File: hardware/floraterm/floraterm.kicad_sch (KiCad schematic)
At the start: 3 parts, among them U1 TMUX1104DGSR, U2 TMUX1104DGSR

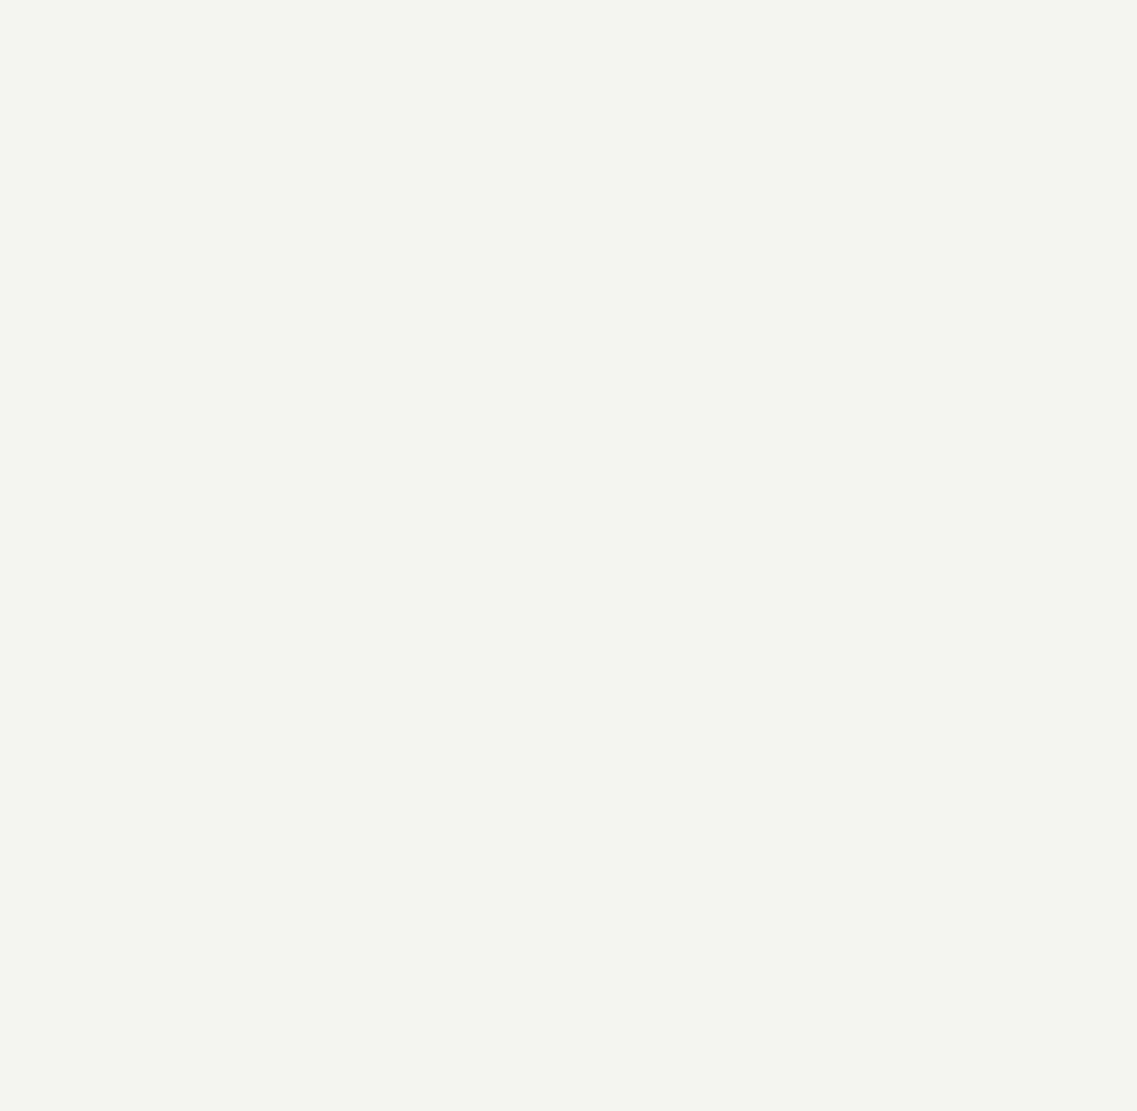
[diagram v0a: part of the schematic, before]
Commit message: add dcdc and bat chrg
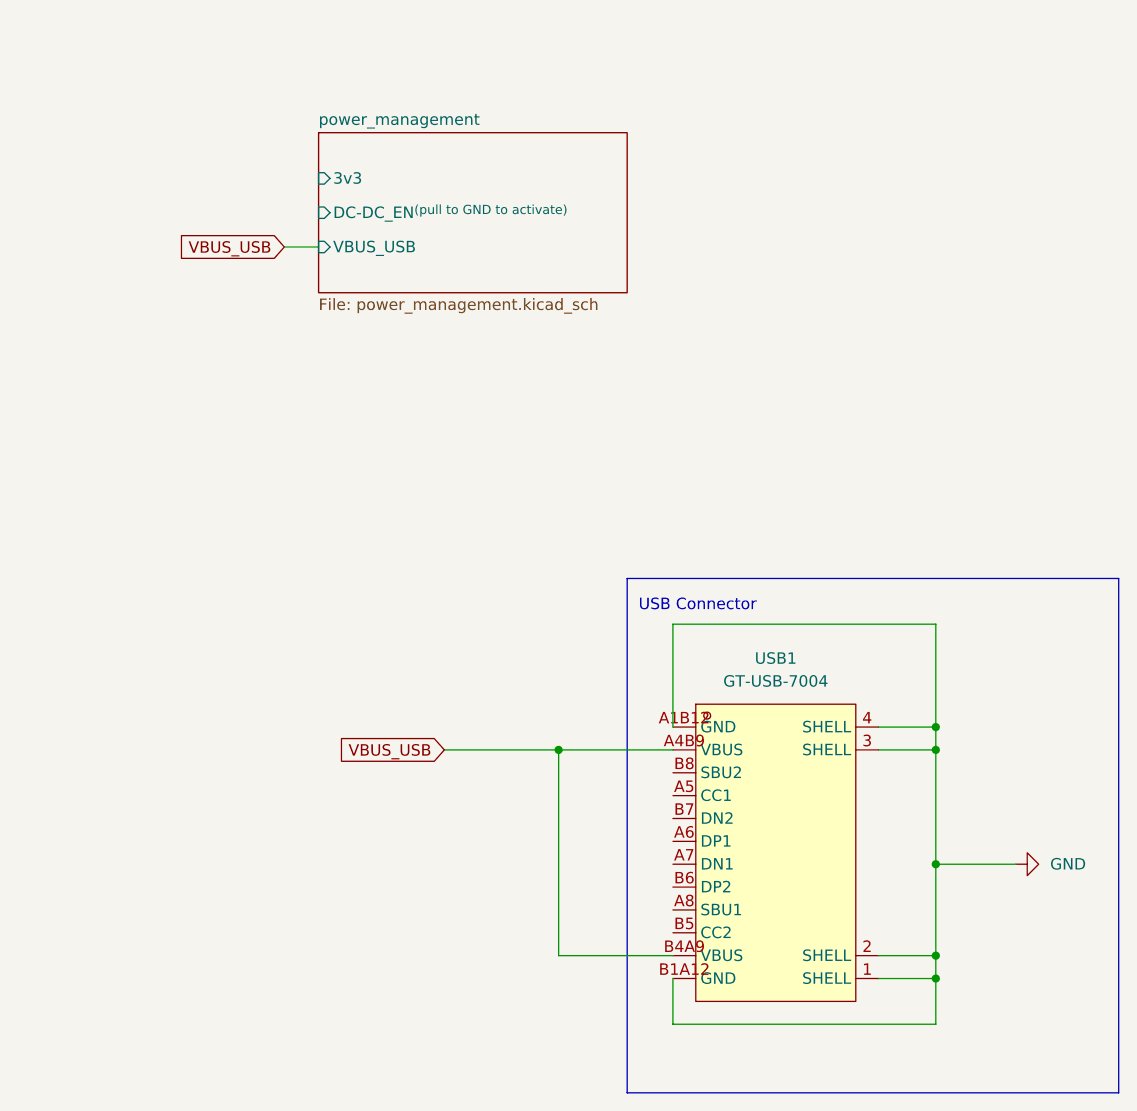
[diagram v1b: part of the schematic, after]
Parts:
- added USB1: GT-USB-7004, lcsc:USB-C-SMD_GT-USB-7004, symbol lcsc:GT-USB-7004
- 1: footprint (none) -> M1s:M1s
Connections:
- new net GND: USB1.1 (SHELL), USB1.2 (SHELL), USB1.3 (SHELL), USB1.4 (SHELL), USB1.A1B12 (GND), USB1.B1A12 (GND)
- new net VBUS_USB: USB1.A4B9 (VBUS), USB1.B4A9 (VBUS)
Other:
- added sheet power_management (power_management.kicad_sch)
- note added: "USB Connector"
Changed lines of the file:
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@@
     (rev "1.0.0")
   )
+  (junction (at 374.65 157.48) (diameter 0) (color 0 0 0 0)
+  )
+  (junction (at 374.65 154.94) (diameter 0) (color 0 0 0 0)
+  )
+  (junction (at 374.65 180.34) (diameter 0) (color 0 0 0 0)
+  )
+  (junction (at 332.74 157.48) (diameter 0) (color 0 0 0 0)
+  )
+  (junction (at 374.65 182.88) (diameter 0) (color 0 0 0 0)
+  )
+  (junction (at 374.65 170.18) (diameter 0) (color 0 0 0 0)
+  )
+  (wire (pts (xy 374.65 157.48) (xy 374.65 170.18))
+    (stroke (width 0) (type default))
+  )
+  (wire (pts (xy 374.65 170.18) (xy 374.65 180.34))
+    (stroke (width 0) (type default))
+  )
+  (wire (pts (xy 345.44 143.51) (xy 374.65 143.51))
+    (stroke (width 0) (type default))
+  )
+  (wire (pts (xy 368.3 180.34) (xy 374.65 180.34))
+    (stroke (width 0) (type default))
+  )
+  (wire (pts (xy 368.3 157.48) (xy 374.65 157.48))
+    (stroke (width 0) (type default))
+  )
+  (wire (pts (xy 345.44 180.34) (xy 332.74 180.34))
+    (stroke (width 0) (type default))
+  )
+  (wire (pts (xy 368.3 154.94) (xy 374.65 154.94))
+    (stroke (width 0) (type default))
+  )
+  (wire (pts (xy 345.44 154.94) (xy 345.44 143.51))
+    (stroke (width 0) (type default))
+  )
+  (wire (pts (xy 368.3 182.88) (xy 374.65 182.88))
+    (stroke (width 0) (type default))
+  )
+  (wire (pts (xy 374.65 154.94) (xy 374.65 157.48))
+    (stroke (width 0) (type default))
+  )
+  (wire (pts (xy 332.74 180.34) (xy 332.74 157.48))
+    (stroke (width 0) (type default))
+  )
+  (wire (pts (xy 374.65 170.18) (xy 383.54 170.18))
+    (stroke (width 0) (type default))
+  )
+  (wire (pts (xy 345.44 187.96) (xy 374.65 187.96))
+    (stroke (width 0) (type default))
+  )
+  (wire (pts (xy 374.65 180.34) (xy 374.65 182.88))
+    (stroke (width 0) (type default))
+  )
+  (wire (pts (xy 374.65 143.51) (xy 374.65 154.94))
+    (stroke (width 0) (type default))
+  )
+  (wire (pts (xy 345.44 182.88) (xy 345.44 187.96))
+    (stroke (width 0) (type default))
+  )
+  (wire (pts (xy 320.04 157.48) (xy 332.74 157.48))
+    (stroke (width 0) (type default))
+  )
+  (wire (pts (xy 302.26 101.6) (xy 306.07 101.6))
+    (stroke (width 0) (type default))
+  )
+  (wire (pts (xy 374.65 182.88) (xy 374.65 187.96))
+    (stroke (width 0) (type default))
+  )
+  (wire (pts (xy 332.74 157.48) (xy 345.44 157.48))
+    (stroke (width 0) (type default))
+  )
+  (rectangle (start 340.36 138.43) (end 394.97 195.58)
+    (stroke (width 0) (type default))
+    (fill (type none))
+  )
   (rectangle (start 39.37 85.09) (end 99.06 161.29)
     (stroke (width 0) (type default))
     (fill (type none))
+  )
+  (text "USB Connector" (at 341.63 142.24 0)
+    (effects (font (size 1.27 1.27)) (justify left bottom))
   )
   (text "SPI mux for screen" (at 43.18 91.44 0)
     (effects (font (size 1.27 1.27)) (justify left bottom))
+  )
+  (global_label "VBUS_USB" (shape input) (at 320.04 157.48 180) (fields_autoplaced)
+    (effects (font (size 1.27 1.27)) (justify right))
+    (property "Intersheetrefs" "${INTERSHEET_REFS}" (at 307.3786 157.48 0)
+      (effects (font (size 1.27 1.27)) (justify right) hide)
+    )
+  )
+  (global_label "VBUS_USB" (shape input) (at 302.26 101.6 180) (fields_autoplaced)
+    (effects (font (size 1.27 1.27)) (justify right))
+    (property "Intersheetrefs" "${INTERSHEET_REFS}" (at 289.5986 101.6 0)
+      (effects (font (size 1.27 1.27)) (justify right) hide)
+    )
   )
   (symbol (lib_id "lcsc:TMUX1104DGSR") (at 66.04 114.3 0) (unit 1)
@@
     )
   )
+  (symbol (lib_id "power:GND") (at 383.54 170.18 90) (unit 1)
+    (in_bom yes) (on_board yes) (dnp no) (fields_autoplaced)
+    (property "Reference" "#PWR09" (at 389.89 170.18 0)
+      (effects (font (size 1.27 1.27)) hide)
+    )
+    (property "Value" "GND" (at 387.35 170.18 90)
+      (effects (font (size 1.27 1.27)) (justify right))
+    )
+    (property "Footprint" "" (at 383.54 170.18 0)
+      (effects (font (size 1.27 1.27)) hide)
+    )
+    (property "Datasheet" "" (at 383.54 170.18 0)
+      (effects (font (size 1.27 1.27)) hide)
+    )
+    (pin "1")
+    (instances
+      (project "floraterm"
+        (path "/3fcab154-9951-4e3b-a2fc-1f8584ec05da"
+          (reference "#PWR09") (unit 1)
+        )
+      )
+    )
+  )
   (symbol (lib_id "lcsc:TMUX1104DGSR") (at 64.77 142.24 0) (unit 1)
     (in_bom yes) (on_board yes) (dnp no) (fields_autoplaced)
@@
       (effects (font (size 1.27 1.27)))
     )
-    (property "Footprint" "" (at 162.56 191.77 0)
+    (property "Footprint" "M1s:M1s" (at 162.56 191.77 0)
       (effects (font (size 1.27 1.27)) hide)
     )
@@
       )
     )
+  )
+  (symbol (lib_id "lcsc:GT-USB-7004") (at 358.14 170.18 0) (unit 1)
+    (in_bom yes) (on_board yes) (dnp no) (fields_autoplaced)
+    (property "Reference" "USB1" (at 356.87 147.32 0)
+      (effects (font (size 1.27 1.27)))
+    )
+    (property "Value" "GT-USB-7004" (at 356.87 149.86 0)
+      (effects (font (size 1.27 1.27)))
+    )
+    (property "Footprint" "lcsc:USB-C-SMD_GT-USB-7004" (at 358.14 190.5 0)
+      (effects (font (size 1.27 1.27)) hide)
+    )
+    (property "Datasheet" "" (at 358.14 170.18 0)
+      (effects (font (size 1.27 1.27)) hide)
+    )
+    (property "LCSC Part" "C2686968" (at 358.14 193.04 0)
+      (effects (font (size 1.27 1.27)) hide)
+    )
+    (pin "B1A12")
+    (pin "B5")
+    (pin "A8")
+    (pin "A1B12")
+    (pin "A5")
+    (pin "A7")
+    (pin "1")
+    (pin "B8")
+    (pin "A6")
+    (pin "B6")
+    (pin "4")
+    (pin "2")
+    (pin "3")
+    (pin "B4A9")
+    (pin "B7")
+    (pin "A4B9")
+    (instances
+      (project "floraterm"
+        (path "/3fcab154-9951-4e3b-a2fc-1f8584ec05da"
+          (reference "USB1") (unit 1)
+        )
+      )
+    )
+  )
+  (sheet (at 306.07 88.9) (size 34.29 17.78) (fields_autoplaced)
+    (stroke (width 0.1524) (type solid))
+    (fill (color 0 0 0 0.0000))
+    (property "Sheetname" "power_management" (at 306.07 88.1884 0)
+      (effects (font (size 1.27 1.27)) (justify left bottom))
+    )
+    (property "Sheetfile" "power_management.kicad_sch" (at 306.07 107.2646 0)
+      (effects (font (size 1.27 1.27)) (justify left top))
+    )
+    (pin "3v3" input (at 306.07 93.98 180)
+      (effects (font (size 1.27 1.27)) (justify left))
+    )
+    (pin "DC-DC_EN^{(pull to GND to activate)}" input (at 306.07 97.79 180)
+      (effects (font (size 1.27 1.27)) (justify left))
+    )
+    (pin "VBUS_USB" input (at 306.07 101.6 180)
+      (effects (font (size 1.27 1.27)) (justify left))
+    )
+    (instances
+      (project "floraterm"
+        (path "/3fcab154-9951-4e3b-a2fc-1f8584ec05da" (page "2"))
+      )
+    )

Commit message: add rp2040
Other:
- added sheet RP2040 (rp2040.kicad_sch)
- moved on the sheet: 1
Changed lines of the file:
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@@
     )
   )
-  (symbol (lib_id "M1s:0_M1s") (at 162.56 191.77 0) (unit 1)
+  (symbol (lib_id "M1s:0_M1s") (at 158.75 149.86 0) (unit 1)
     (in_bom yes) (on_board yes) (dnp no) (fields_autoplaced)
-    (property "Reference" "1" (at 173.99 77.47 0)
+    (property "Reference" "1" (at 170.18 35.56 0)
       (effects (font (size 1.27 1.27)))
     )
-    (property "Value" "0_M1s" (at 173.99 80.01 0)
+    (property "Value" "0_M1s" (at 170.18 38.1 0)
       (effects (font (size 1.27 1.27)))
     )
-    (property "Footprint" "M1s:M1s" (at 162.56 191.77 0)
+    (property "Footprint" "M1s:M1s" (at 158.75 149.86 0)
       (effects (font (size 1.27 1.27)) hide)
     )
-    (property "Datasheet" "" (at 162.56 191.77 0)
+    (property "Datasheet" "" (at 158.75 149.86 0)
       (effects (font (size 1.27 1.27)) hide)
     )
@@
       )
     )
+  )
+  (sheet (at 335.28 40.64) (size 36.83 24.13) (fields_autoplaced)
+    (stroke (width 0.1524) (type solid))
+    (fill (color 0 0 0 0.0000))
+    (property "Sheetname" "RP2040" (at 335.28 39.9284 0)
+      (effects (font (size 1.27 1.27)) (justify left bottom))
+    )
+    (property "Sheetfile" "rp2040.kicad_sch" (at 335.28 65.3546 0)
+      (effects (font (size 1.27 1.27)) (justify left top))
+    )
+    (pin "spi_cs" input (at 335.28 43.18 180)
+      (effects (font (size 1.27 1.27)) (justify left))
+    )
+    (pin "tft_bl" input (at 335.28 45.72 180)
+      (effects (font (size 1.27 1.27)) (justify left))
+    )
+    (pin "spi_clk" input (at 335.28 48.26 180)
+      (effects (font (size 1.27 1.27)) (justify left))
+    )
+    (pin "spi_mosi" input (at 335.28 50.8 180)
+      (effects (font (size 1.27 1.27)) (justify left))
+    )
+    (pin "spi_rst" input (at 335.28 53.34 180)
+      (effects (font (size 1.27 1.27)) (justify left))
+    )
+    (pin "spi_dc" input (at 335.28 55.88 180)
+      (effects (font (size 1.27 1.27)) (justify left))
+    )
+    (pin "spi_mux_2" input (at 335.28 58.42 180)
+      (effects (font (size 1.27 1.27)) (justify left))
+    )
+    (pin "spi_mux_1" input (at 335.28 60.96 180)
+      (effects (font (size 1.27 1.27)) (justify left))
+    )
+    (instances
+      (project "floraterm"
+        (path "/3fcab154-9951-4e3b-a2fc-1f8584ec05da" (page "3"))
+      )
+    )

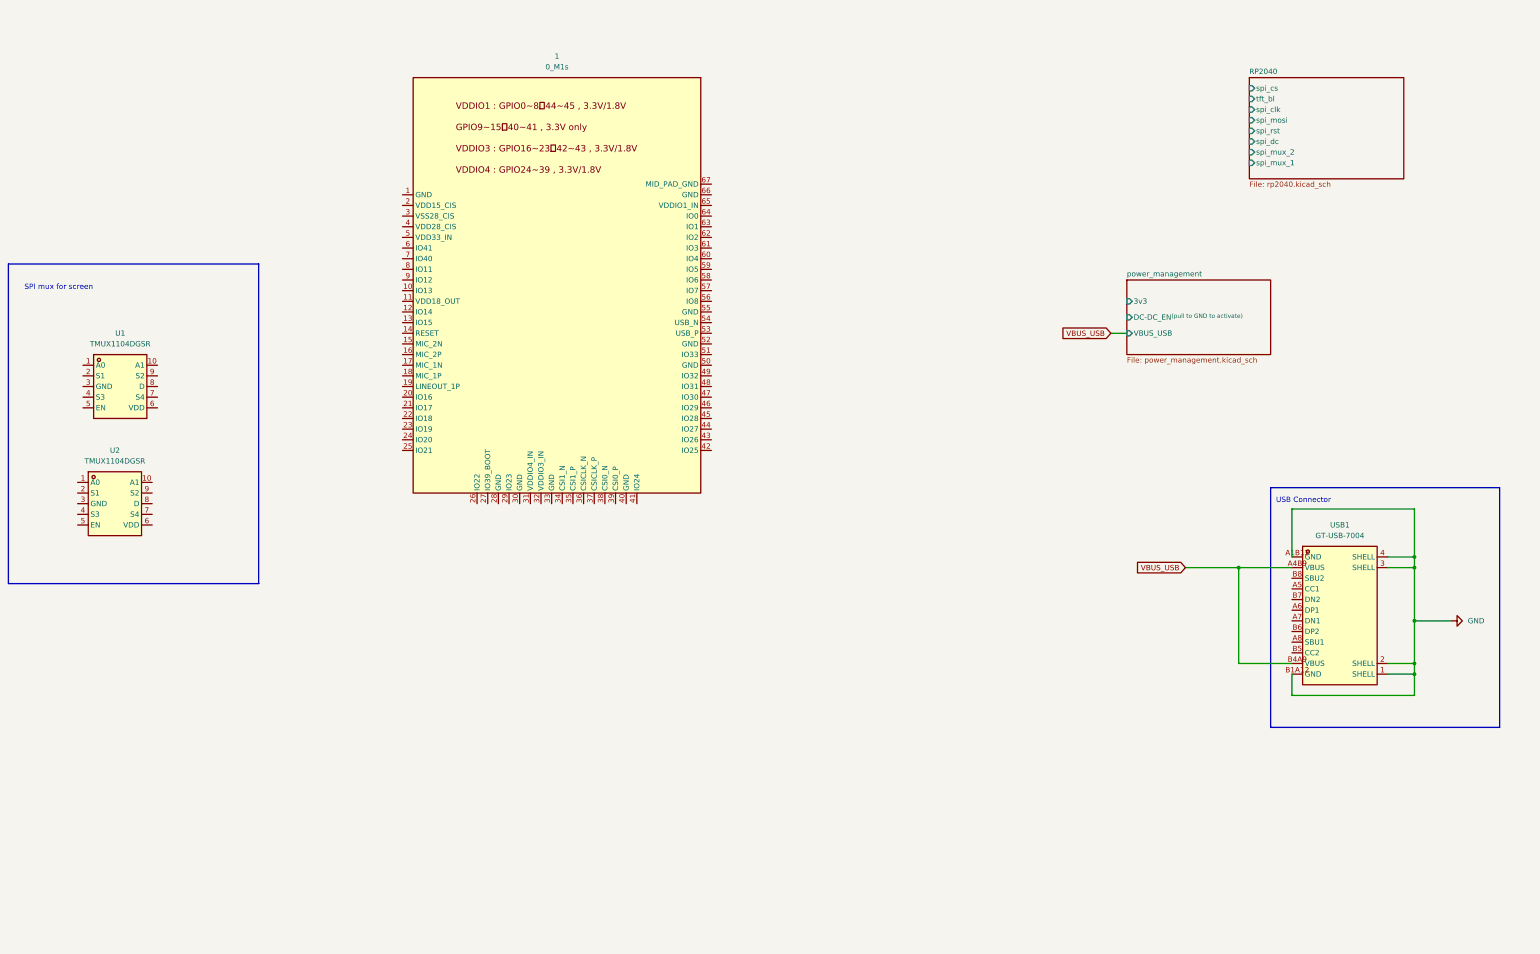
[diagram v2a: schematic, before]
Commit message: add screen, keyboard and speaker
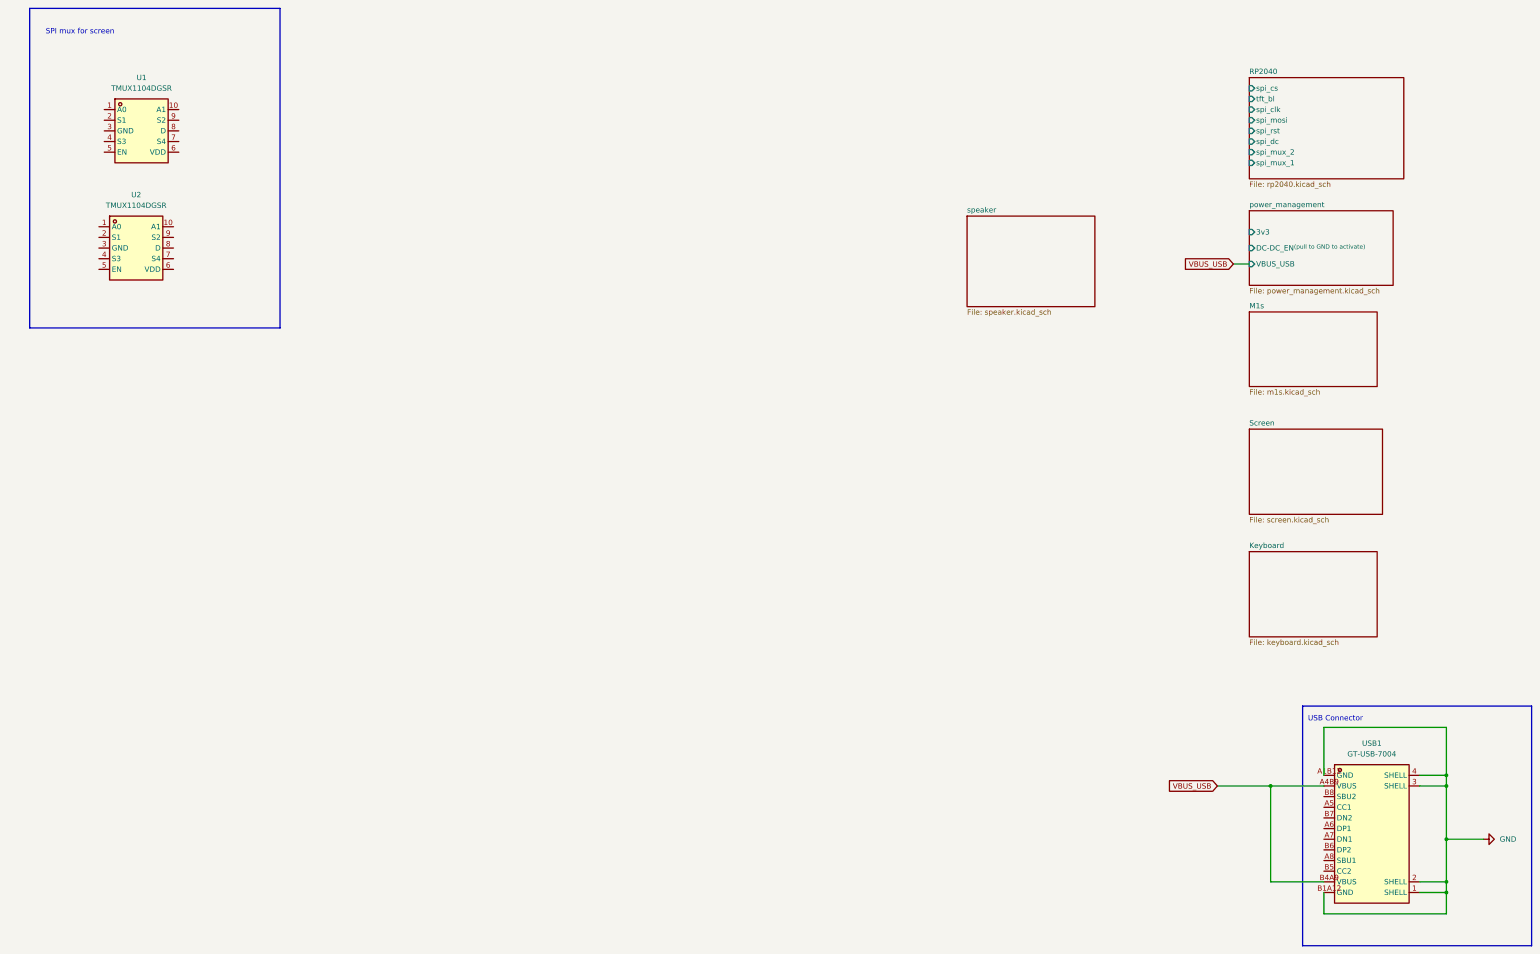
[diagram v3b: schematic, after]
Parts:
- removed 1: 0_M1s, M1s:M1s, symbol M1s:0_M1s
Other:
- added sheet Keyboard (keyboard.kicad_sch)
- added sheet M1s (m1s.kicad_sch)
- added sheet Screen (screen.kicad_sch)
- added sheet speaker (speaker.kicad_sch)
- moved on the sheet: U1, U2, USB1
